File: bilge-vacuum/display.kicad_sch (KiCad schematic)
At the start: 8 parts, among them Q5 PMV65XP,215, U12 NHD-C12864A1Z-FSW-FBW-HTT

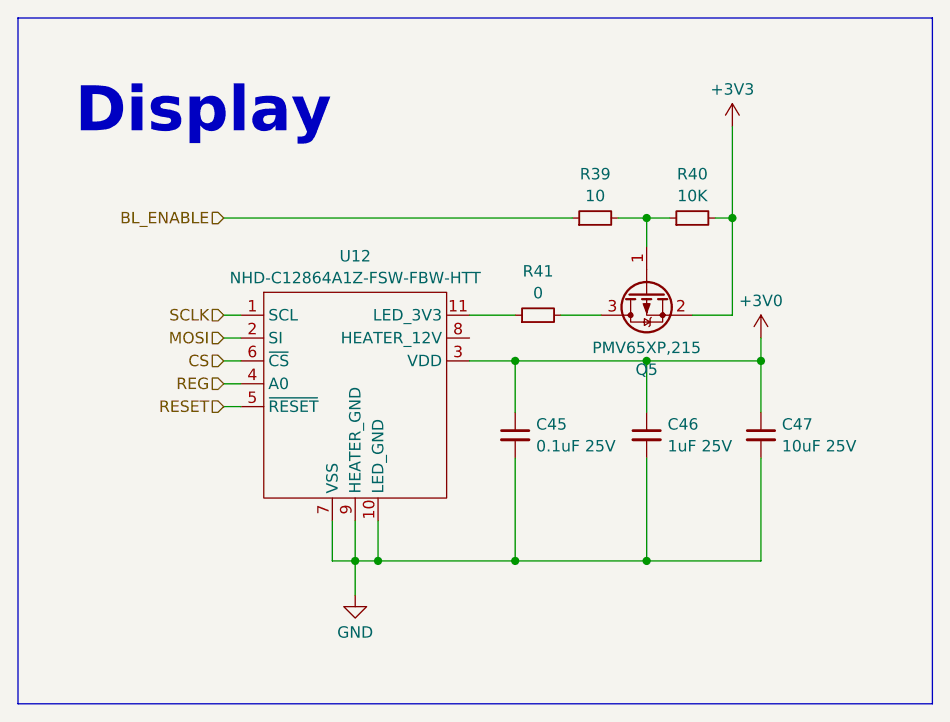
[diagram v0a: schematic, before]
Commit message: Assign the bulk of parts, some passives still need custom footprints.
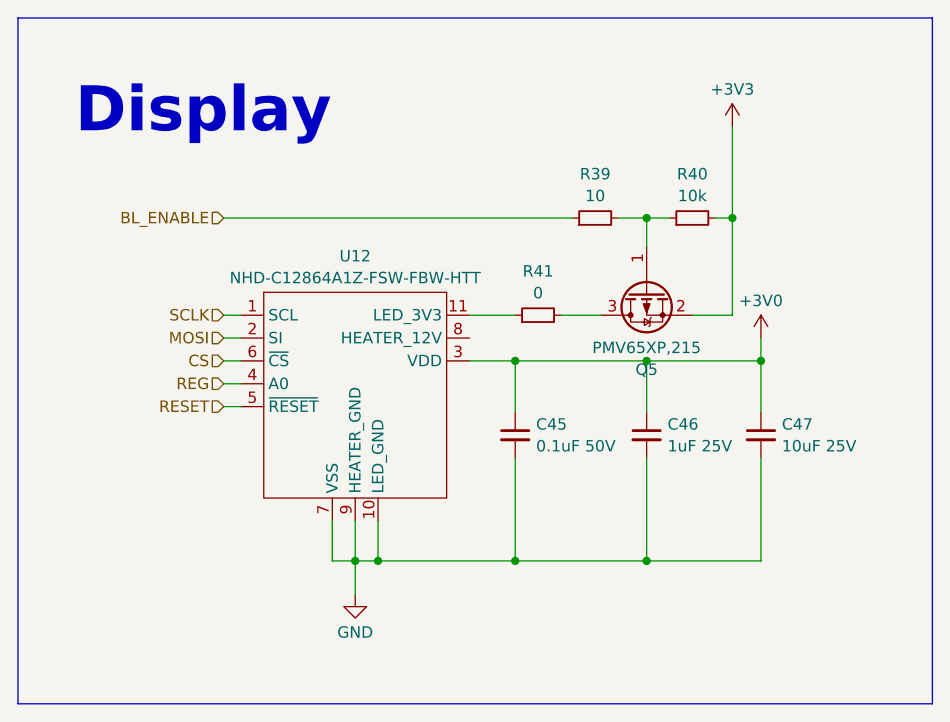
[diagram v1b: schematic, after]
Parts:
- C45: value 0.1uF 25V -> 0.1uF 50V; footprint (none) -> Capacitor_SMD:C_0805_2012Metric
- C46: footprint (none) -> Capacitor_SMD:C_0805_2012Metric
- C47: footprint (none) -> Capacitor_SMD:C_1206_3216Metric
- Q5: footprint (none) -> Package_TO_SOT_SMD:SOT-23-3
- R39, R41: footprint (none) -> Resistor_SMD:R_0805_2012Metric
- R40: value 10K -> 10k; footprint (none) -> Resistor_SMD:R_0805_2012Metric
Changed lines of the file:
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@@
       (effects (font (size 1.27 1.27)) (justify left))
     )
-    (property "Value" "0.1uF 25V" (at 76.6191 66.6234 0)
-      (effects (font (size 1.27 1.27)) (justify left))
-    )
-    (property "Footprint" "" (at 74.295 65.405 0)
+    (property "Value" "0.1uF 50V" (at 76.6191 66.6234 0)
+      (effects (font (size 1.27 1.27)) (justify left))
+    )
+    (property "Footprint" "Capacitor_SMD:C_0805_2012Metric" (at 74.295 65.405 0)
       (effects (font (size 1.27 1.27)) hide)
     )
@@
       (effects (font (size 1.27 1.27)))
     )
-    (property "Value" "10K" (at 93.98 38.8183 90)
-      (effects (font (size 1.27 1.27)))
-    )
-    (property "Footprint" "" (at 93.98 41.275 0)
+    (property "Value" "10k" (at 93.98 38.8183 90)
+      (effects (font (size 1.27 1.27)))
+    )
+    (property "Footprint" "Resistor_SMD:R_0805_2012Metric" (at 93.98 41.275 0)
       (effects (font (size 1.27 1.27)) hide)
     )
@@
       (effects (font (size 1.27 1.27)))
     )
-    (property "Footprint" "" (at 83.185 41.275 0)
+    (property "Footprint" "Resistor_SMD:R_0805_2012Metric" (at 83.185 41.275 0)
       (effects (font (size 1.27 1.27)) hide)
     )
@@
       (effects (font (size 1.27 1.27)) (justify left))
     )
-    (property "Footprint" "" (at 88.9 65.405 0)
+    (property "Footprint" "Capacitor_SMD:C_0805_2012Metric" (at 88.9 65.405 0)
       (effects (font (size 1.27 1.27)) hide)
     )
@@
       (effects (font (size 1.27 1.27)))
     )
-    (property "Footprint" "" (at 86.36 54.61 0)
+    (property "Footprint" "Package_TO_SOT_SMD:SOT-23-3" (at 86.36 54.61 0)
       (effects (font (size 1.27 1.27)) hide)
     )
@@
       (effects (font (size 1.27 1.27)) (justify left))
     )
-    (property "Footprint" "" (at 101.6 65.405 0)
+    (property "Footprint" "Capacitor_SMD:C_1206_3216Metric" (at 101.6 65.405 0)
       (effects (font (size 1.27 1.27)) hide)
     )
@@
       (effects (font (size 1.27 1.27)))
     )
-    (property "Footprint" "" (at 76.835 52.07 0)
-      (effects (font (size 1.27 1.27)) hide)
-    )
+    (property "Footprint" "Resistor_SMD:R_0805_2012Metric" (at 76.835 52.07 0)
+      (effects (font (size 1.27 1.27)) hide)
+    )

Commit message: Fixes
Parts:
- C47: value 10uF 25V -> 10uF 50V
- R40: value 10k -> 10k 1%
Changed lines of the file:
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@@
       (effects (font (size 1.27 1.27)))
     )
-    (property "Value" "10k" (at 93.98 38.8183 90)
+    (property "Value" "10k 1%" (at 93.98 38.8183 90)
       (effects (font (size 1.27 1.27)))
     )
@@
       (effects (font (size 1.27 1.27)) (justify left))
     )
-    (property "Value" "10uF 25V" (at 103.9241 66.6234 0)
-      (effects (font (size 1.27 1.27)) (justify left))
-    )
+    (property "Value" "10uF 50V" (at 103.9241 66.6234 0)
+      (effects (font (size 1.27 1.27)) (justify left))
+    )
